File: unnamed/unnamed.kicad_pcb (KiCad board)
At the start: 2 copper layers, 171.4 x 108.6 mm, 47 parts, among them J1 Serial, SW1 SW_Push, SW10 SW_Push, SW11 SW_Push, SW12 SW_Push, SW13 SW_Push, SW14 SW_Push, SW15 SW_Push, SW16 SW_Push, SW17 SW_Push, SW2 SW_Push, SW3 SW_Push, SW4 SW_Push, SW5 SW_Push, SW6 SW_Push, SW7 SW_Push, SW8 SW_Push, SW9 SW_Push, U2 eliteC

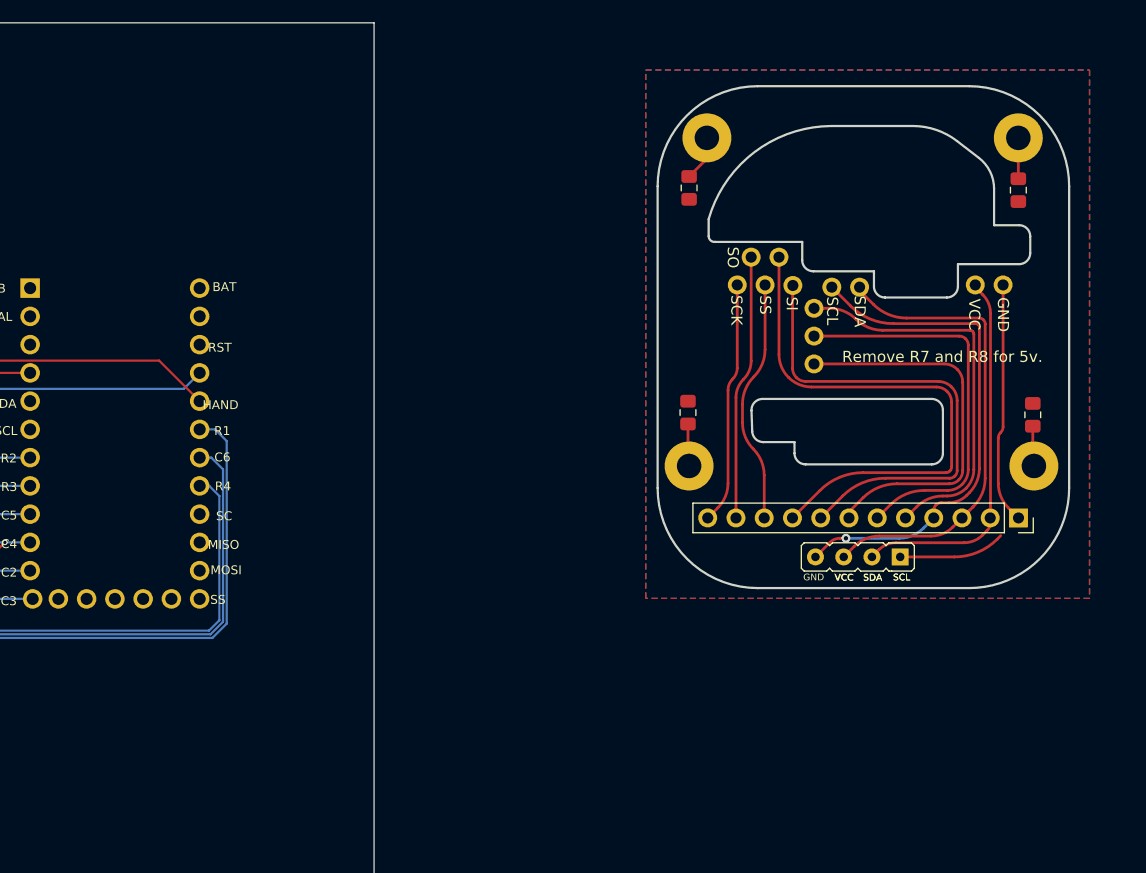
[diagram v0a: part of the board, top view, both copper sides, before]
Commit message: routing, audio jack, rst button
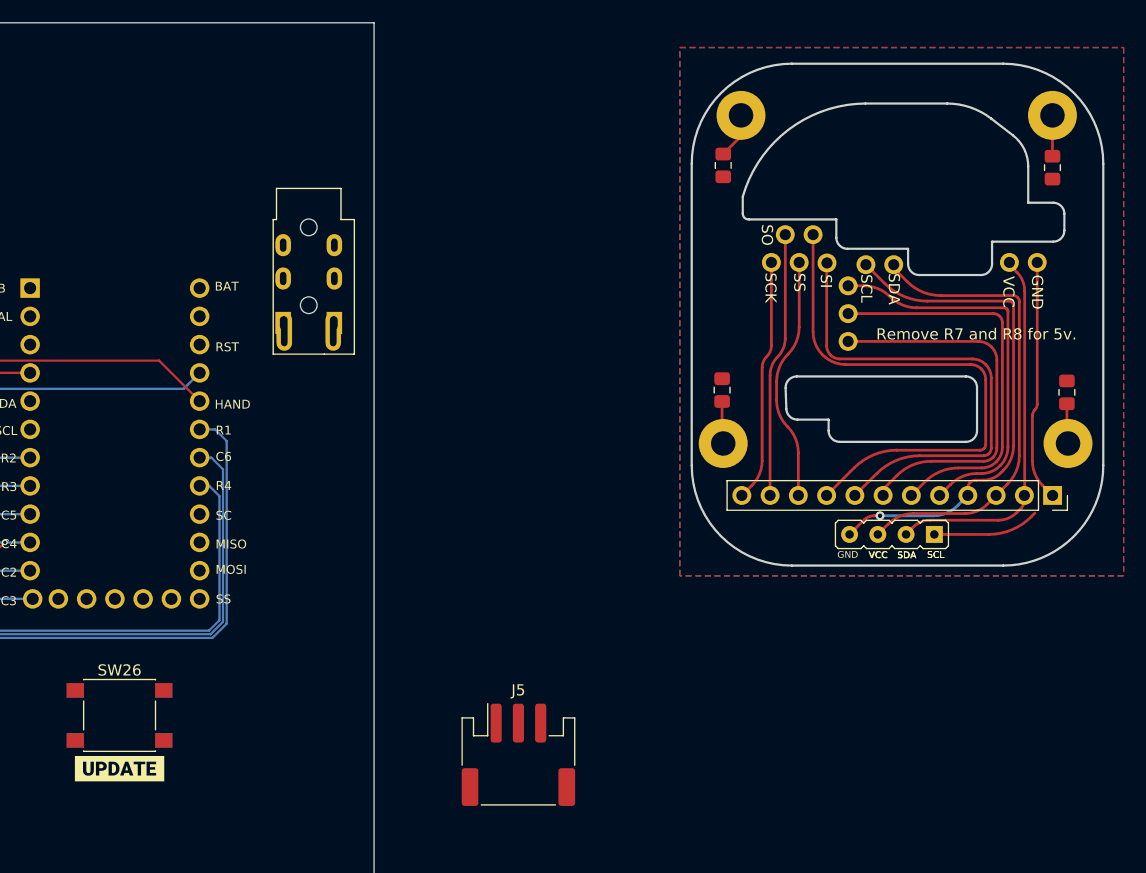
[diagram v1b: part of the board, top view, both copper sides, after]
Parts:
- added J2: Serial, footprints:Jack_3.5mm_PJ320E_Horizontal_reversible, F.Cu at (238.7, 40.1)
- added J5: S3B-PH-SM4-TB(LF)(SN), Connector_JST:JST_PH_S3B-PH-SM4-TB_1x03-1MP_P2.00mm_Horizontal, F.Cu at (259.9, 79.0)
- added SW26: SW_SPST, Button_Switch_SMD:SW_Push_1P1T_NO_6x6mm_H9.5mm, F.Cu at (224.0, 75.4)
- added SW37: SW_SPST, Button_Switch_SMD:SW_Push_1P1T_NO_6x6mm_H9.5mm, B.Cu at (224.0, 75.4)
- added kibuzzard-61F01C84: G***, kibuzzard-61F01C84, F.Cu at (224.0, 80.2)
- added kibuzzard-61F01C84: G***, kibuzzard-61F01C84, B.Cu at (224.0, 80.3)
- moved FB1 3.67 mm to (307.9, 26.2)
- moved FB2 3.67 mm to (278.3, 26.0)
- moved FB3 3.67 mm to (278.2, 46.2)
- moved FB4 3.67 mm to (309.2, 46.4)
- moved H1 3.67 mm to (307.9, 21.5)
- moved H2 3.67 mm to (279.9, 21.5)
- moved H3 3.67 mm to (278.3, 51.0)
- moved H4 3.67 mm to (309.3, 51.0)
- moved J1 3.67 mm to (309.9, 59.3)
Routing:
- net col5_l: track 95.7 -> 131.2 mm
- net mosi_l: track 35.6 -> 0.00 mm

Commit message: routing
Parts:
- added kibuzzard-628D396A: G***, kibuzzard-628D396A, F.Cu at (234.3, 44.4)
- added kibuzzard-628D3A32: G***, kibuzzard-628D3A32, F.Cu at (217.4, 91.3)
- added kibuzzard-628D3A32: G***, kibuzzard-628D3A32, B.Cu at (217.4, 91.3)
- added kibuzzard-628D3AA1: G***, kibuzzard-628D3AA1, B.Cu at (234.3, 44.4)
- R7, R8: footprint footprints:D_1206_handsolder -> footprints:R_1206_handsolder
- SW26, SW37: footprint Button_Switch_SMD:SW_Push_1P1T_NO_6x6mm_H9.5mm -> footprints:SW_Push_1P1T_NO_6x6mm_H9.5mm
- moved R7 33.3 mm to (241.1, 47.6)
- moved R8 33.3 mm to (241.1, 47.6)
- moved kibuzzard-61F01C84 25.3 mm to (227.4, 55.2), turned to -90 degrees
- moved kibuzzard-61F01C84 25.2 mm to (227.4, 55.2), turned to 90 degrees
- moved SW26 20.4 mm to (222.6, 55.1), turned to 90 degrees
- moved SW37 20.4 mm to (222.6, 55.1), turned to -90 degrees
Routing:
- net Gnd_l: track 7.97 -> 109.0 mm, vias 0 -> 2
- net sda_l: track 0.00 -> 55.2 mm
- net scl_l: track 0.00 -> 53.9 mm
- net Vcc_l: track 24.2 -> 75.4 mm
- net hand: track 26.9 -> 12.6 mm
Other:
- board text added: "5.1k"
- board text added: "5V"
- board text added: "GND"
- board text added: "S"
- board text added: "hands"

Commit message: add jlc stuff
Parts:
- moved FB2 72.2 mm to (210.7, 51.2)
- moved H3 72.2 mm to (210.7, 76.2)
- moved H4 72.2 mm to (241.7, 76.2)
- moved FB3 72.2 mm to (210.6, 71.4)
- moved FB4 72.2 mm to (241.6, 71.6)
- moved J1 72.2 mm to (242.3, 84.6)
- moved FB1 72.2 mm to (240.3, 51.4)
- moved H1 72.2 mm to (240.3, 46.7)
- moved H2 72.2 mm to (212.3, 46.7)
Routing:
- net (no net): track 278.9 -> 257.1 mm
- net col3_l: track 161.7 -> 183.5 mm

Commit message: edge cuts
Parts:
- moved H3 53.0 mm to (258.9, 54.2)
- moved H4 53.0 mm to (289.9, 54.2)
- moved FB2 53.0 mm to (258.9, 29.2)
- moved FB3 53.0 mm to (258.8, 49.4)
- moved FB4 53.0 mm to (289.8, 49.6)
- moved J1 53.0 mm to (290.5, 62.5)
- moved FB1 53.0 mm to (288.5, 29.4)
- moved H1 53.0 mm to (288.5, 24.7)
- moved H2 53.0 mm to (260.5, 24.7)
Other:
- board size 171.4 x 108.6 mm -> 142.3 x 95.1 mm

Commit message: holes
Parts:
- added H1: M4, footprints:MountingHole_3mm_Pad_thin, F.Cu at (142.9, 28.8)
- added H2: M4, footprints:MountingHole_3mm_Pad_thin, F.Cu at (243.2, 92.0)
- added H3: M4, footprints:MountingHole_3mm_Pad_thin, F.Cu at (207.8, 37.0)
- added H4: M4, footprints:MountingHole_3mm_Pad_thin, F.Cu at (125.9, 87.1)
- added H5: M4, footprints:MountingHole_3mm_Pad_thin, F.Cu at (178.4, 86.5)
- H1000: renamed from H1; value MountingHole_Pad -> M4; footprint BK-CirqueDB:MountingHole_2.2mm_M2_Pad -> footprints:MountingHole_3mm_Pad_thin
- H20000 : renamed from H2; value MountingHole_Pad -> M4; footprint BK-CirqueDB:MountingHole_2.2mm_M2_Pad -> footprints:MountingHole_3mm_Pad_thin
- H3000: renamed from H3; value MountingHole_Pad -> M4; footprint BK-CirqueDB:MountingHole_2.2mm_M2_Pad -> footprints:MountingHole_3mm_Pad_thin
- H4000: renamed from H4; value MountingHole_Pad -> M4; footprint BK-CirqueDB:MountingHole_2.2mm_M2_Pad -> footprints:MountingHole_3mm_Pad_thin
- moved FB1 60.7 mm to (349.1, 26.7)
- moved FB2 60.7 mm to (319.5, 26.5)
- moved FB3 60.7 mm to (319.4, 46.7)
- moved FB4 60.7 mm to (350.4, 46.9)
- moved H1000 60.7 mm to (349.1, 22.0)
- moved H20000  60.7 mm to (321.1, 22.0)
- moved H3000 60.7 mm to (319.5, 51.5)
- moved H4000 60.7 mm to (350.5, 51.5)
- moved J1 60.7 mm to (351.1, 59.8)
- moved D5 8.72 mm to (124.2, 80.7)
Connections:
- H1000 pad 1: (no net) -> GND
- H20000  pad 1: (no net) -> GND
- H3000 pad 1: (no net) -> GND
- H4000 pad 1: (no net) -> GND
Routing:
- net (no net): track 257.1 -> 241.9 mm
- net GND: track 0.00 -> 15.2 mm
- net col1_l: track 185.5 -> 176.8 mm
- net Net-(D5-Pad2): track 25.3 -> 28.5 mm
